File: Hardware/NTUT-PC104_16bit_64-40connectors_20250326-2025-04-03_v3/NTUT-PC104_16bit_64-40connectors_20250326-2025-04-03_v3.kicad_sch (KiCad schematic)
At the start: 41 parts, among them J10 Conn_02x26_Odd_Even, J12 Conn_02x04_Odd_Even, J13 Conn_02x04_Odd_Even, J14 Conn_02x04_Odd_Even, J15 Conn_02x04_Odd_Even, J16 Conn_02x04_Odd_Even, J17 Conn_02x04_Odd_Even, J18 Conn_02x04_Odd_Even, J7 Conn_02x04_Odd_Even, J8 Conn_02x26_Odd_Even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

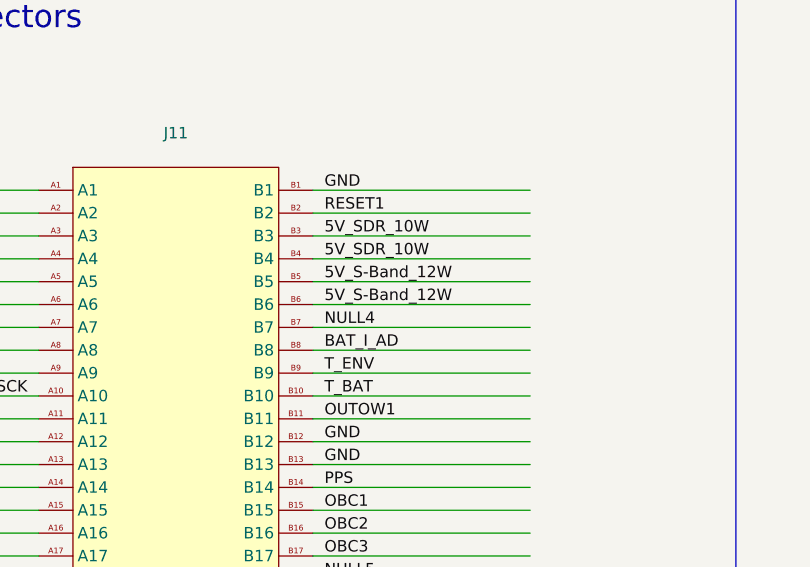
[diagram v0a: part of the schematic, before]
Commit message: 1. Connections between J5-J11 done. 2. Correct upper/lower case of J11.
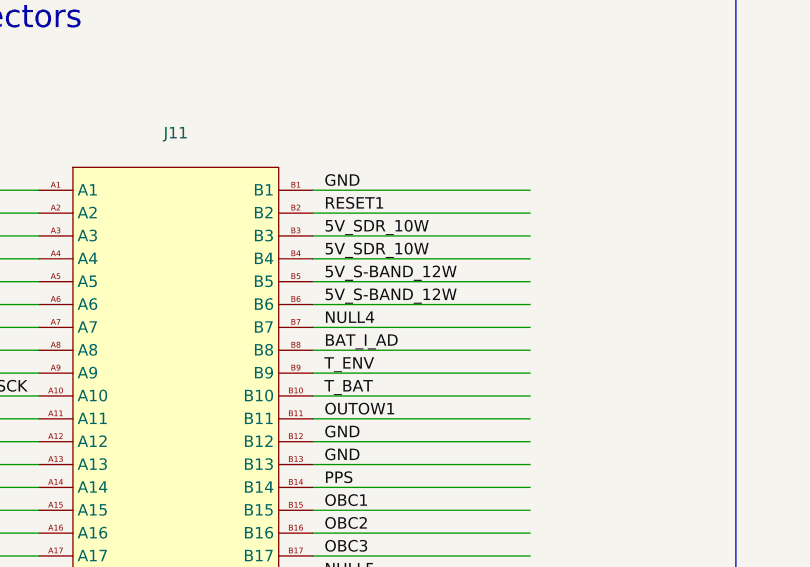
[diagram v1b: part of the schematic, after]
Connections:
- net 5V_S-Band_12W is gone; now on net 5V_S-BAND_12W: J11.B5, J11.B6
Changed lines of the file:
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@@
 		)
 	)
-	(label "5V_S-Band_12W"
+	(label "5V_S-BAND_12W"
 		(at 308.61 227.33 0)
 		(effects
@@
 		)
 	)
-	(label "5V_S-Band_12W"
+	(label "5V_S-BAND_12W"
 		(at 308.61 224.79 0)
 		(effects

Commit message: 1. 9.0.0 works ok.  Cause of net mess up was the zones.  Remove zones    solve the problem. 2. upper portion is almost done.
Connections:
- net OUTOW1 is gone; now on net OUTPW1: J1.B11, J11.B11, J2.B11, J3.B11, J4.B11, J5.B11, J6.B11, J9.22 (Pin_22), JA19.22 (Pin_22)
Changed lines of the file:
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@@
 		)
 	)
-	(label "OUTOW1"
+	(label "OUTPW1"
 		(at 488.95 60.96 0)
 		(effects
@@
 		)
 	)
-	(label "OUTOW1"
+	(label "OUTPW1"
 		(at 163.83 243.84 0)
 		(effects
@@
 		)
 	)
-	(label "OUTOW1"
+	(label "OUTPW1"
 		(at 163.83 60.96 0)
 		(effects
@@
 		)
 	)
-	(label "OUTOW1"
+	(label "OUTPW1"
 		(at 81.28 60.96 0)
 		(effects
@@
 		)
 	)
-	(label "OUTOW1"
+	(label "OUTPW1"
 		(at 245.11 60.96 0)
 		(effects
@@
 		)
 	)
-	(label "OUTOW1"
+	(label "OUTPW1"
 		(at 73.66 243.84 0)
 		(effects
@@
 		)
 	)
-	(label "OUTOW1"
+	(label "OUTPW1"
 		(at 308.61 240.03 0)
 		(effects
@@
 		)
 	)
-	(label "OUTOW1"
+	(label "OUTPW1"
 		(at 327.66 60.96 0)
 		(effects
@@
 		)
 	)
-	(label "OUTOW1"
+	(label "OUTPW1"
 		(at 406.4 60.96 0)
 		(effects

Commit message: 1. Layout completed. 2. Isolated copper zone ignored. 3. Needs to validate and verify the layout completely.
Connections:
- net OUTPW1: no longer J1.B11, J11.B11, J2.B11, J3.B11, J4.B11, J5.B11, J6.B11, J9.22 (Pin_22), JA19.22 (Pin_22)
- new net OUTPW1_1: J1.B11, J11.B11, J2.B11, J3.B11, J4.B11, J5.B11, J6.B11, J9.22 (Pin_22), JA19.22 (Pin_22)
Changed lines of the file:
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@@
 		)
 	)
-	(label "OUTPW1"
+	(label "OUTPW1_1"
 		(at 488.95 60.96 0)
 		(effects
@@
 		)
 	)
-	(label "OUTPW1"
+	(label "OUTPW1_1"
 		(at 163.83 243.84 0)
 		(effects
@@
 		)
 	)
-	(label "OUTPW1"
+	(label "OUTPW1_1"
 		(at 163.83 60.96 0)
 		(effects
@@
 		)
 	)
-	(label "OUTPW1"
+	(label "OUTPW1_1"
 		(at 81.28 60.96 0)
 		(effects
@@
 		)
 	)
-	(label "OUTPW1"
+	(label "OUTPW1_1"
 		(at 245.11 60.96 0)
 		(effects
@@
 		)
 	)
-	(label "OUTPW1"
+	(label "OUTPW1_1"
 		(at 73.66 243.84 0)
 		(effects
@@
 		)
 	)
-	(label "OUTPW1"
+	(label "OUTPW1_1"
 		(at 308.61 240.03 0)
 		(effects
@@
 		)
 	)
-	(label "OUTPW1"
+	(label "OUTPW1_1"
 		(at 327.66 60.96 0)
 		(effects
@@
 		)
 	)
-	(label "OUTPW1"
+	(label "OUTPW1_1"
 		(at 406.4 60.96 0)
 		(effects
